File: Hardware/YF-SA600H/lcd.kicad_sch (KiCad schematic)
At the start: 26 parts, among them Q1 Q_NPN_BEC

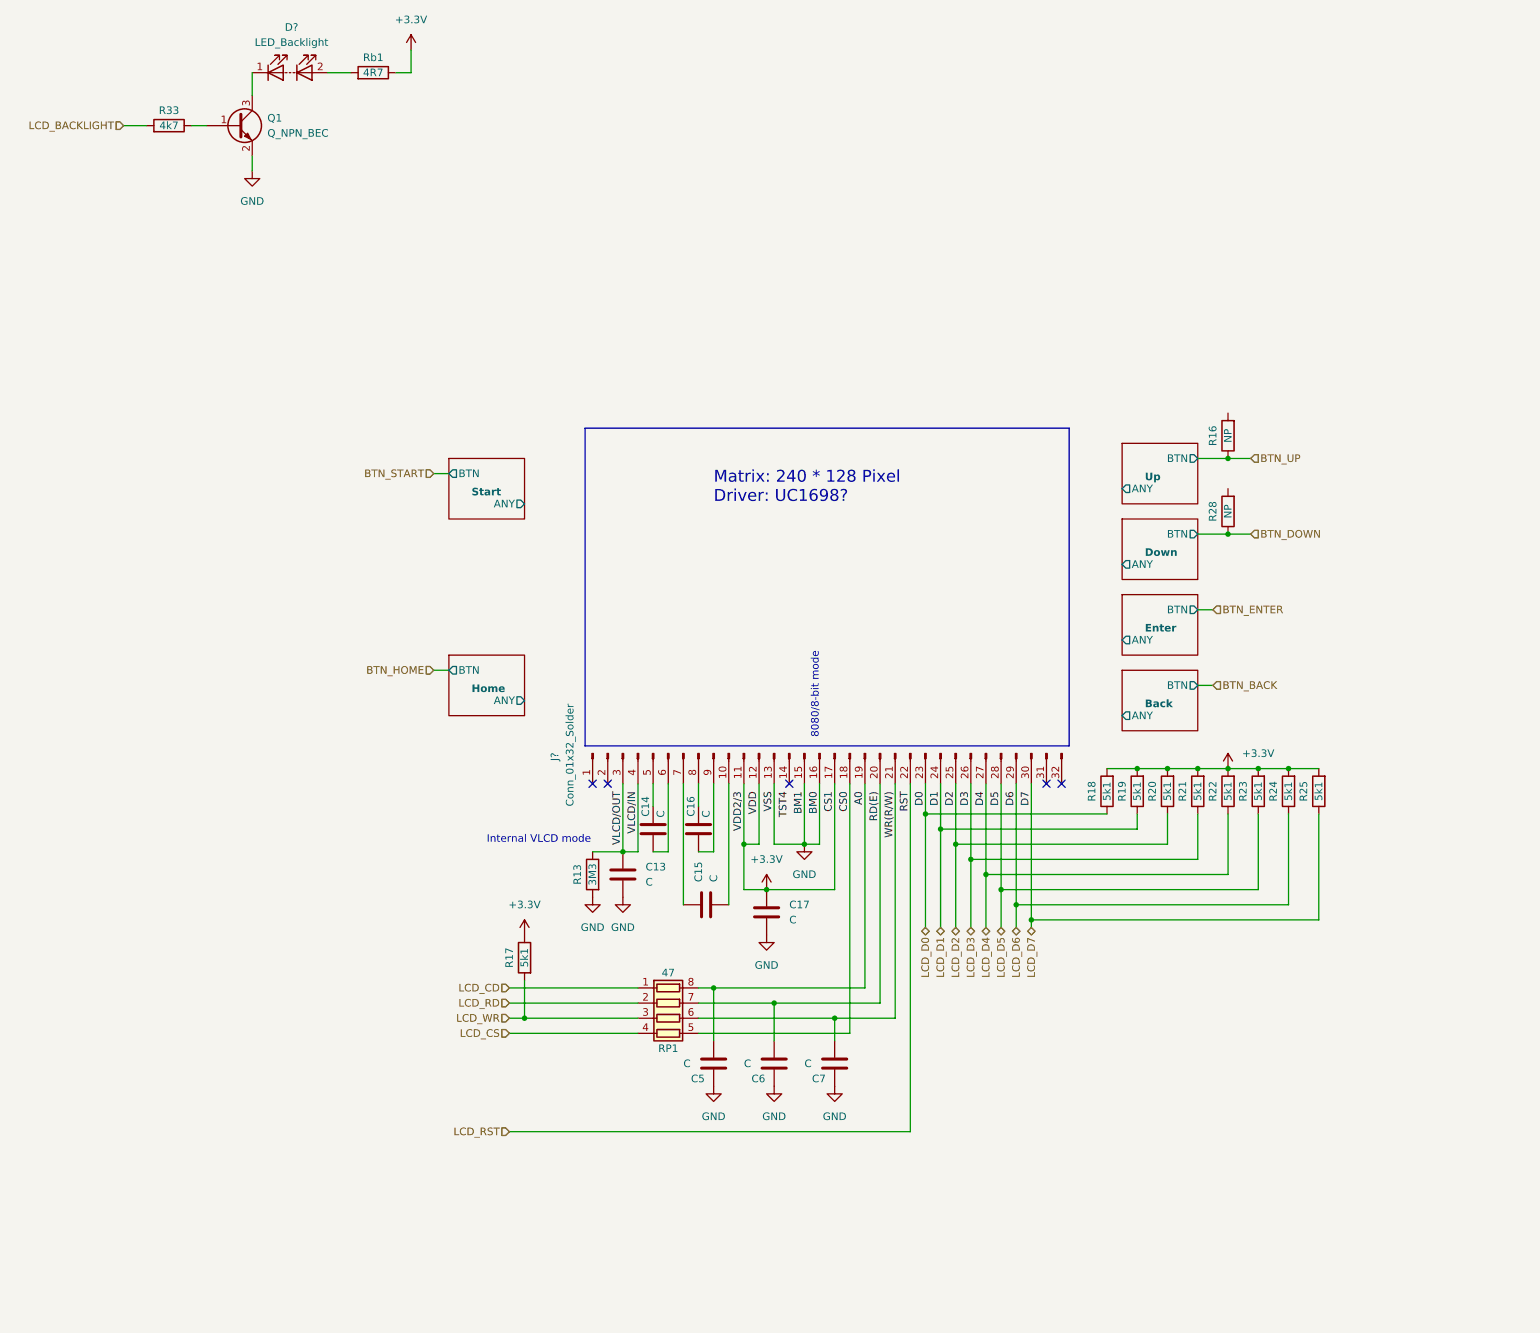
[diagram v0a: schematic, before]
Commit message: Add buttons
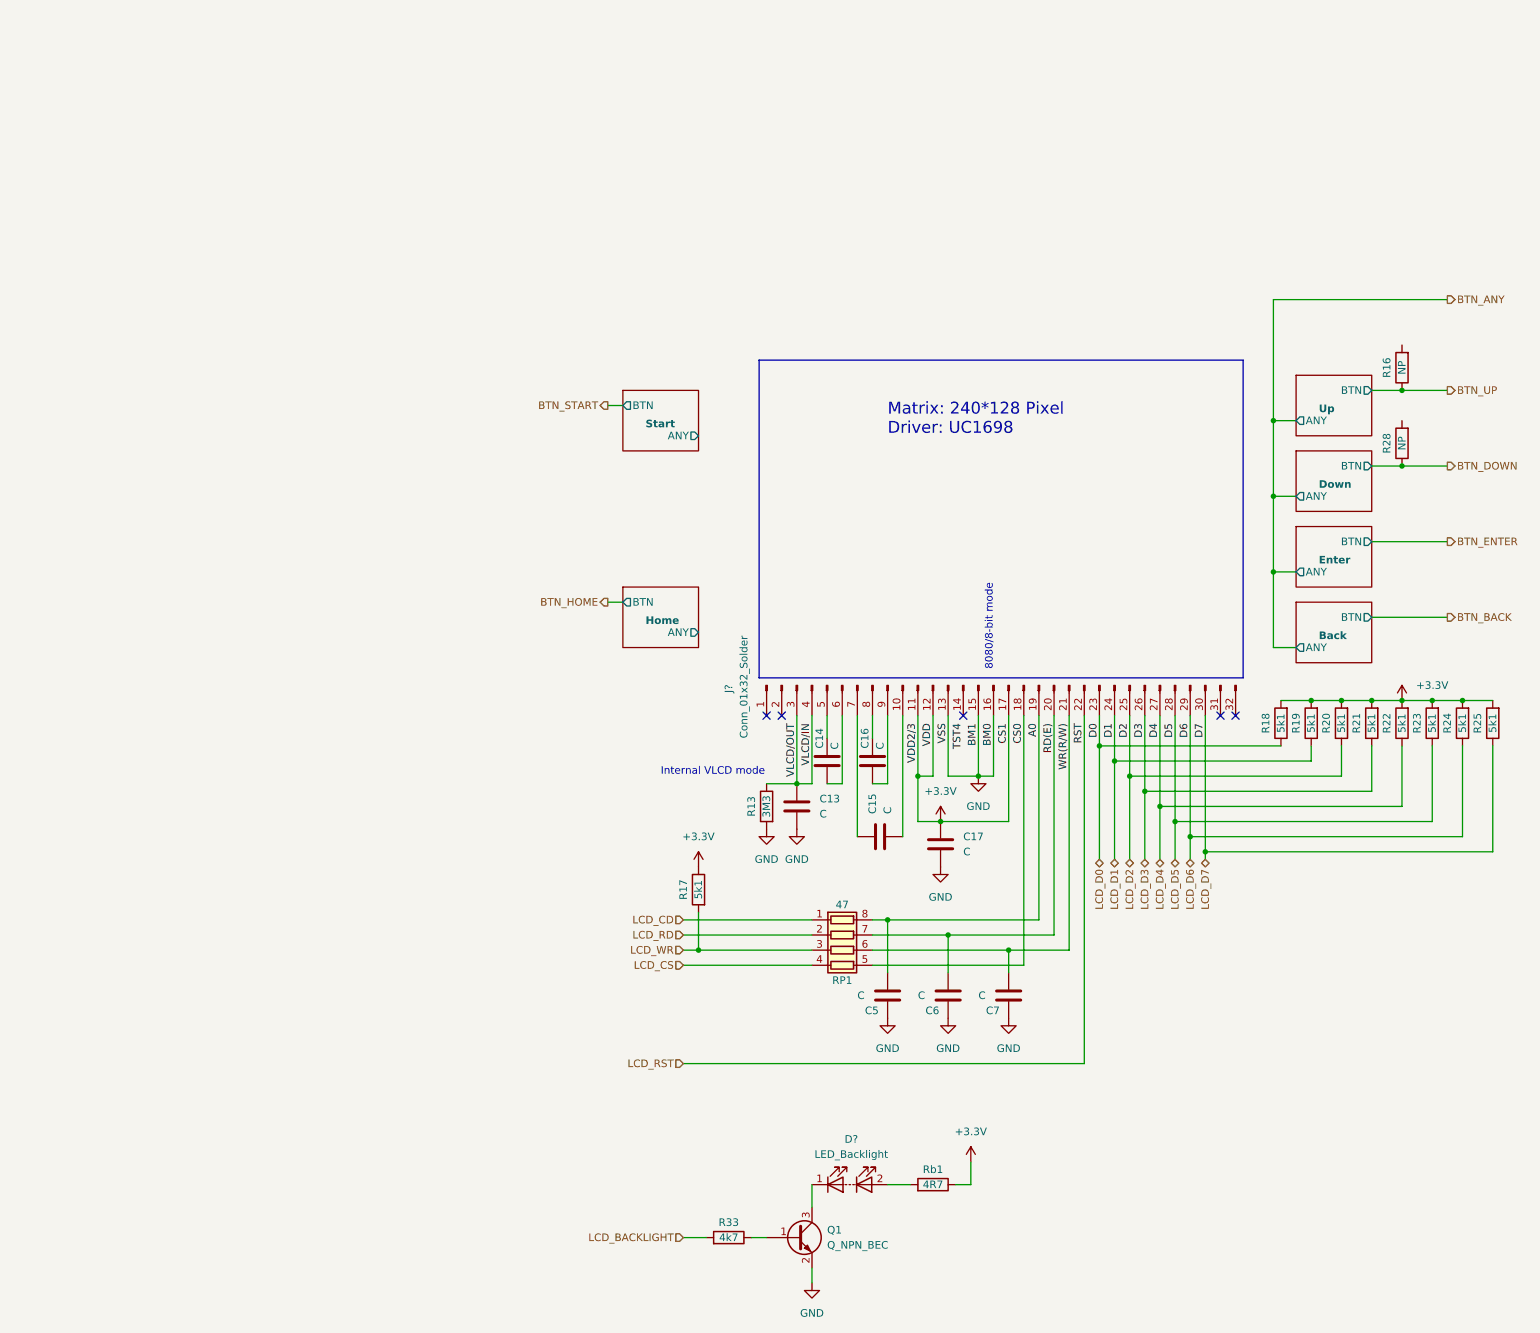
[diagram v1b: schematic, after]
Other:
- note added: "Matrix: 240*128 Pixel Driver: UC1698"
- note removed: "Matrix: 240 * 128 Pixel Driver: UC1698?"
- title: (none) -> YardForce SAxxxPRO Dot-Matrix LCD CoverUI HS49067
- moved on the sheet: C13, C14, C15, C16, C17, C5, C6, C7, D?, J?, Q1, R13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
